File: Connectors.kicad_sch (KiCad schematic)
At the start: 6 parts, among them J2 USB_C_Receptacle_USB2.0_16P, J5 Conn_01x02_Socket, J6 Conn_01x02_Socket, U3 USBLC6-2SC6

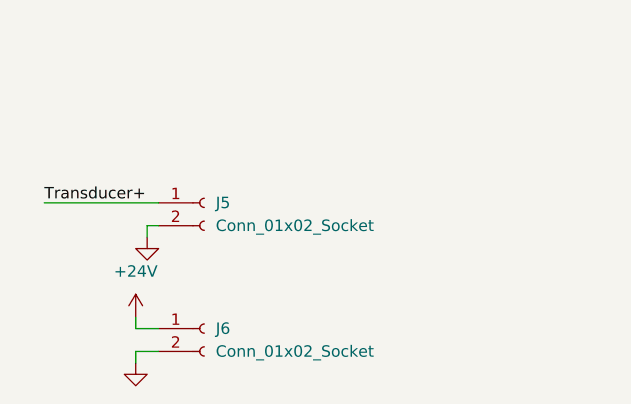
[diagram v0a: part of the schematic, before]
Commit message: Changes before syncing to main. Adding crystal as well as Thermocouple sensor and buck 3.3V step down
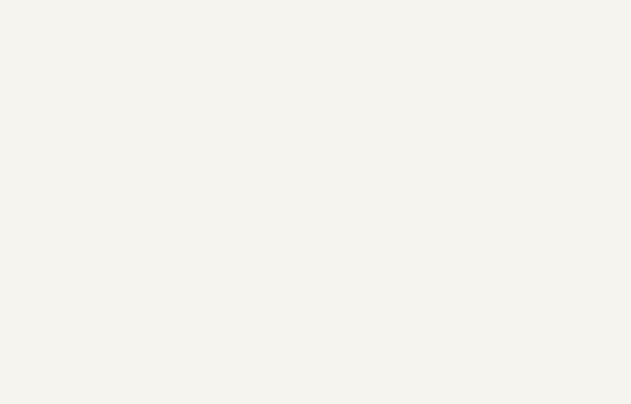
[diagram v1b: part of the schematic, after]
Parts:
- removed J5, J6: Conn_01x02_Socket, symbol Connector:Conn_01x02_Socket
